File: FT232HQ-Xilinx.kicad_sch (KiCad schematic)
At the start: 33 parts, among them J1 USB_C_Receptacle_USB2.0_16P, J2 Conn_02x07_Odd_Even, J3 Conn_02x05_Odd_Even, U1 TLV9061xDBV, U2 TLV75533PDBV, U3 SN74AVC4T774PW, U4 12M, U5 FT232H, U6 93LCxxBxxOT

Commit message: fix: 1. Add 10k between vref and gnd. 2. Remove vias on pads.
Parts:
- added R1: 10k, Resistor_SMD:R_0402_1005Metric, symbol Device:R
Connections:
- net GND: now also R1.2
- net VREF: now also R1.1
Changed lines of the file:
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@@
 	)
 	(junction
+		(at 207.01 115.57)
+		(diameter 0)
+		(color 0 0 0 0)
+	)
+	(junction
 		(at 193.04 148.59)
 		(diameter 0)
@@
 	)
 	(junction
+		(at 198.12 105.41)
+		(diameter 0)
+		(color 0 0 0 0)
+	)
+	(junction
 		(at 248.92 107.95)
 		(diameter 0)
@@
 	(wire
 		(pts
+			(xy 198.12 107.95) (xy 198.12 105.41)
+		)
+		(stroke
+			(width 0)
+			(type default)
+		)
+	)
+	(wire
+		(pts
 			(xy 52.07 124.46) (xy 63.5 124.46)
 		)
@@
 	(wire
 		(pts
+			(xy 198.12 115.57) (xy 207.01 115.57)
+		)
+		(stroke
+			(width 0)
+			(type default)
+		)
+	)
+	(wire
+		(pts
 			(xy 142.24 132.08) (xy 144.78 132.08)
 		)
@@
 	(wire
 		(pts
+			(xy 198.12 105.41) (xy 201.93 105.41)
+		)
+		(stroke
+			(width 0)
+			(type default)
+		)
+	)
+	(wire
+		(pts
 			(xy 259.08 43.18) (xy 260.35 43.18)
 		)
@@
 	)
 	(symbol
+		(lib_id "Device:R")
+		(at 198.12 111.76 0)
+		(unit 1)
+		(exclude_from_sim no)
+		(in_bom yes)
+		(on_board yes)
+		(dnp no)
+		(property "Reference" "R1"
+			(at 197.358 114.3 90)
+			(effects
+				(font
+					(size 1.27 1.27)
+				)
+				(justify right)
+			)
+		)
+		(property "Value" "10k"
+			(at 198.12 110.236 90)
+			(effects
+				(font
+					(size 1.27 1.27)
+				)
+				(justify right)
+			)
+		)
+		(property "Footprint" "Resistor_SMD:R_0402_1005Metric"
+			(at 196.342 111.76 90)
+			(effects
+				(font
+					(size 1.27 1.27)
+				)
+				(hide yes)
+			)
+		)
+		(property "Datasheet" "~"
+			(at 198.12 111.76 0)
+			(effects
+				(font
+					(size 1.27 1.27)
+				)
+				(hide yes)
+			)
+		)
+		(property "Description" "Resistor"
+			(at 198.12 111.76 0)
+			(effects
+				(font
+					(size 1.27 1.27)
+				)
+				(hide yes)
+			)
+		)
+		(pin "2"
+		)
+		(pin "1"
+		)
+		(instances
+			(project "FT232HQ-Xilinx"
+				(path "/dd4ac3e3-2410-4273-be8c-634c81d8b6b2"
+					(reference "R1")
+					(unit 1)
+				)
+			)
+		)
+	)
+	(symbol
 		(lib_id "power:+3V3")
 		(at 242.57 130.81 90)
@@
 	(symbol
 		(lib_id "power:VCC")
-		(at 201.93 105.41 90)
+		(at 198.12 105.41 90)
 		(unit 1)
 		(exclude_from_sim no)
@@
 		(fields_autoplaced yes)
 		(property "Reference" "#PWR010"
-			(at 205.74 105.41 0)
+			(at 201.93 105.41 0)
 			(effects
 				(font
@@
 		)
 		(property "Value" "VREF"
-			(at 198.12 105.4099 90)
+			(at 194.31 105.4099 90)
 			(effects
 				(font
@@
 		)
 		(property "Footprint" ""
-			(at 201.93 105.41 0)
+			(at 198.12 105.41 0)
 			(effects
 				(font
@@
 		)
 		(property "Datasheet" ""
-			(at 201.93 105.41 0)
+			(at 198.12 105.41 0)
 			(effects
 				(font
@@
 		)
 		(property "Description" "Power symbol creates a global label with name \"VCC\""
-			(at 201.93 105.41 0)
+			(at 198.12 105.41 0)
 			(effects
 				(font

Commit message: update
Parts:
- removed J2: Conn_02x07_Odd_Even, 1st_commonly:Molex_Xilinx_02x07_P2.0mm_Vertical, symbol Connector_Generic:Conn_02x07_Odd_Even
- added C14: 104, Capacitor_SMD:C_0402_1005Metric, symbol Device:C
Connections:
- net +5V: now also C14.1
- net GND: now also C14.2
- no-connect marks 20 -> 17
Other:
- moved on the sheet: R1

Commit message: set ac9 as SLEEP# LED
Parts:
- added D1: LED, LED_SMD:LED_0402_1005Metric, symbol Device:LED
- added R2: 10k, Resistor_SMD:R_0402_1005Metric, symbol Device:R
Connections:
- net +3V3: now also R2.2
- net at U5.33 (ACBUS9): now also D1.1 (K)
- new net: D1.2 (A), R2.1
- no-connect marks 17 -> 16
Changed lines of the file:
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@@
 	)
 	(no_connect
-		(at 160.02 109.22)
-	)
-	(no_connect
 		(at 160.02 86.36)
 	)
@@
 	)
 	(symbol
+		(lib_id "Device:R")
+		(at 171.45 109.22 90)
+		(unit 1)
+		(exclude_from_sim no)
+		(in_bom yes)
+		(on_board yes)
+		(dnp no)
+		(property "Reference" "R2"
+			(at 170.434 107.188 90)
+			(effects
+				(font
+					(size 1.27 1.27)
+				)
+				(justify right)
+			)
+		)
+		(property "Value" "10k"
+			(at 169.926 109.22 90)
+			(effects
+				(font
+					(size 1.27 1.27)
+				)
+				(justify right)
+			)
+		)
+		(property "Footprint" "Resistor_SMD:R_0402_1005Metric"
+			(at 171.45 110.998 90)
+			(effects
+				(font
+					(size 1.27 1.27)
+				)
+				(hide yes)
+			)
+		)
+		(property "Datasheet" "~"
+			(at 171.45 109.22 0)
+			(effects
+				(font
+					(size 1.27 1.27)
+				)
+				(hide yes)
+			)
+		)
+		(property "Description" "Resistor"
+			(at 171.45 109.22 0)
+			(effects
+				(font
+					(size 1.27 1.27)
+				)
+				(hide yes)
+			)
+		)
+		(pin "2"
+		)
+		(pin "1"
+		)
+		(instances
+			(project "FT232HQ-Xilinx"
+				(path "/dd4ac3e3-2410-4273-be8c-634c81d8b6b2"
+					(reference "R2")
+					(unit 1)
+				)
+			)
+		)
+	)
+	(symbol
 		(lib_id "power:VCC")
 		(at 270.51 133.35 270)
@@
 	)
 	(symbol
+		(lib_id "Device:LED")
+		(at 163.83 109.22 0)
+		(unit 1)
+		(exclude_from_sim no)
+		(in_bom yes)
+		(on_board yes)
+		(dnp no)
+		(property "Reference" "D1"
+			(at 163.83 106.68 0)
+			(effects
+				(font
+					(size 1.27 1.27)
+				)
+			)
+		)
+		(property "Value" "LED"
+			(at 163.83 112.522 0)
+			(effects
+				(font
+					(size 1.27 1.27)
+				)
+			)
+		)
+		(property "Footprint" "LED_SMD:LED_0402_1005Metric"
+			(at 163.83 109.22 0)
+			(effects
+				(font
+					(size 1.27 1.27)
+				)
+				(hide yes)
+			)
+		)
+		(property "Datasheet" "~"
+			(at 163.83 109.22 0)
+			(effects
+				(font
+					(size 1.27 1.27)
+				)
+				(hide yes)
+			)
+		)
+		(property "Description" "Light emitting diode"
+			(at 163.83 109.22 0)
+			(effects
+				(font
+					(size 1.27 1.27)
+				)
+				(hide yes)
+			)
+		)
+		(pin "2"
+		)
+		(pin "1"
+		)
+		(instances
+			(project "FT232HQ-Xilinx"
+				(path "/dd4ac3e3-2410-4273-be8c-634c81d8b6b2"
+					(reference "D1")
+					(unit 1)
+				)
+			)
+		)
+	)
+	(symbol
 		(lib_id "Interface_USB:FT232H")
 		(at 137.16 93.98 0)
@@
 					(unit 1)
 				)
+			)
+		)
+	)
+	(symbol
+		(lib_id "power:+5V")
+		(at 175.26 109.22 270)
+		(unit 1)
+		(exclude_from_sim no)
+		(in_bom yes)
+		(on_board yes)
+		(dnp no)
+		(fields_autoplaced yes)
+		(property "Reference" "#PWR018"
+			(at 171.45 109.22 0)
+			(effects
+				(font
+					(size 1.27 1.27)
+				)
+				(hide yes)
+			)
+		)
+		(property "Value" "+3V3"
+			(at 179.07 109.2199 90)
+			(effects
+				(font
+					(size 1.27 1.27)
+				)
+				(justify left)
+			)
+		)
+		(property "Footprint" ""
+			(at 175.26 109.22 0)
+			(effects
+				(font
+					(size 1.27 1.27)
+				)
+				(hide yes)
+			)
+		)
+		(property "Datasheet" ""
+			(at 175.26 109.22 0)
+			(effects
+				(font
+					(size 1.27 1.27)
+				)
+				(hide yes)
+			)
+		)
+		(property "Description" "Power symbol creates a global label with name \"+5V\""
+			(at 175.26 109.22 0)
+			(effects
+				(font
+					(size 1.27 1.27)
+				)
+				(hide yes)
+			)
+		)
+		(pin "1"
+		)
+		(instances
+			(project "FT232HQ-Xilinx"
+				(path "/dd4ac3e3-2410-4273-be8c-634c81d8b6b2"
+					(reference "#PWR018")
+					(unit 1)
+				)

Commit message: remove ldo and useless resistance
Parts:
- removed R11, R12, R9: 10k, Resistor_SMD:R_0402_1005Metric, symbol Device:R
- removed U2: TLV75533PDBV, Package_TO_SOT_SMD:SOT-23-5, symbol Regulator_Linear:TLV75533PDBV
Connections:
- net +3V3: no longer U5.40 (VREGIN)
- net +5V: now also U5.40 (VREGIN)

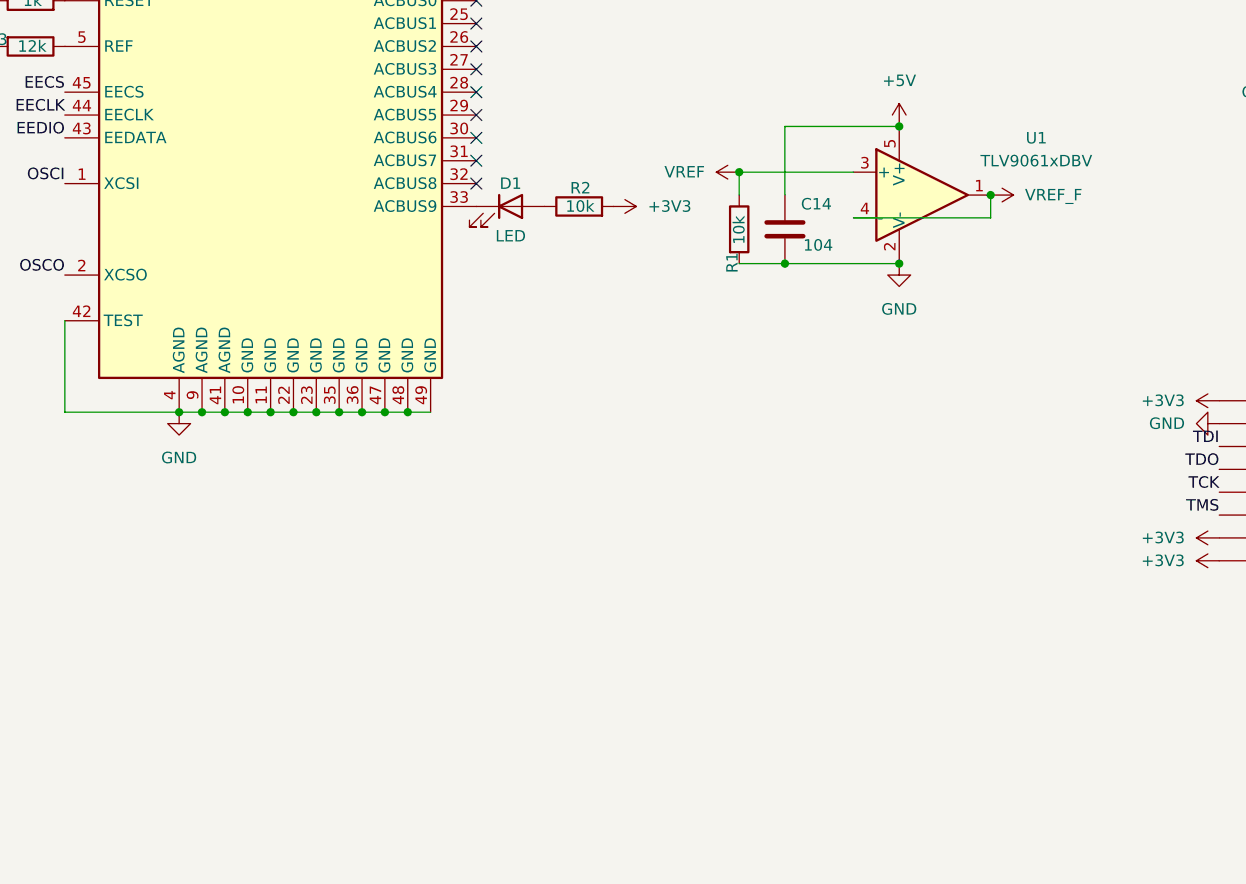
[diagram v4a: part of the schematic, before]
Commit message: add raspberry jst-sh1.0 uart
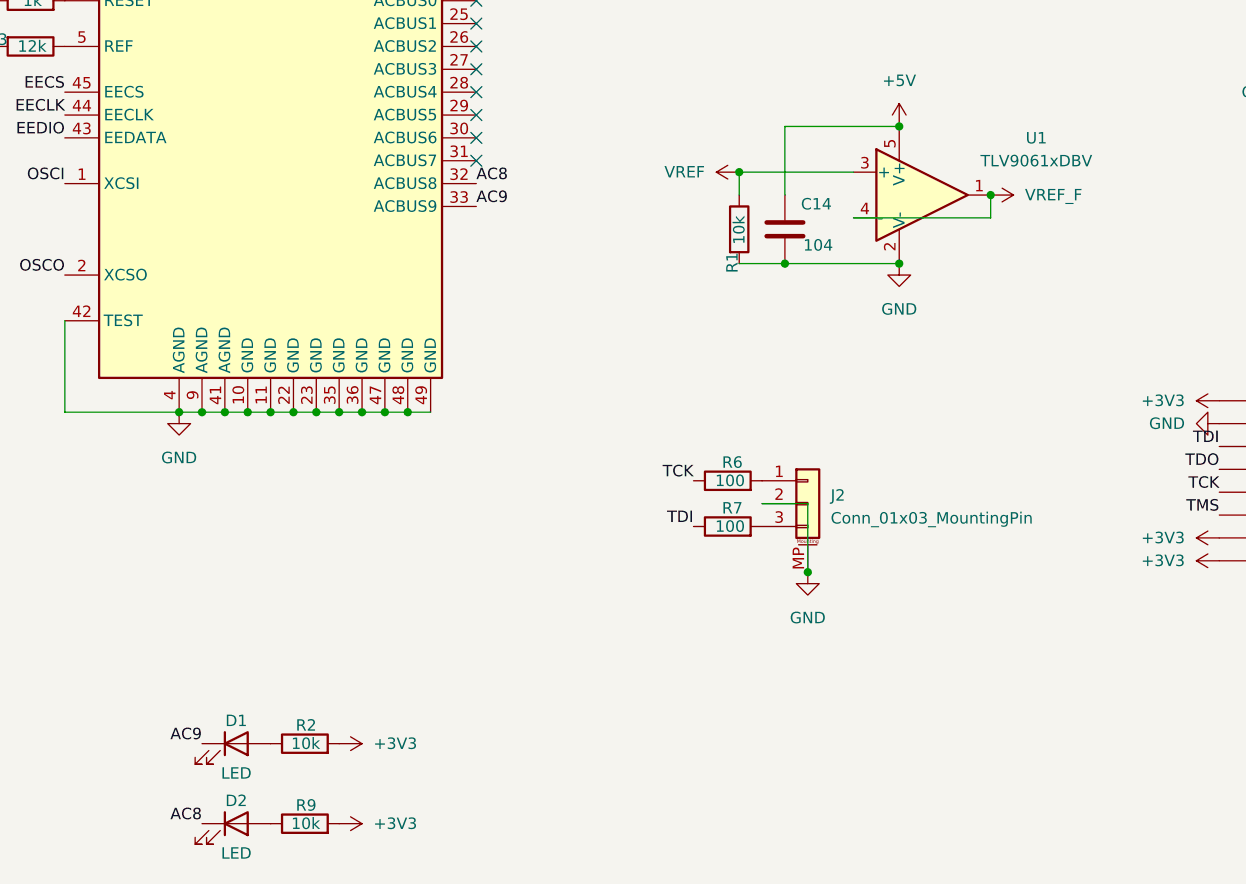
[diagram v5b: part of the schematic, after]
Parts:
- added D2: LED, LED_SMD:LED_0402_1005Metric, symbol Device:LED
- added J2: Conn_01x03_MountingPin, Connector_JST:JST_SH_SM03B-SRSS-TB_1x03-1MP_P1.00mm_Horizontal, symbol Connector_Generic_MountingPin:Conn_01x03_MountingPin
- added R6, R7: 100, Resistor_SMD:R_0402_1005Metric, symbol Device:R
- added R9: 10k, Resistor_SMD:R_0402_1005Metric, symbol Device:R
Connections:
- net +3V3: now also R9.2
- net GND: now also J2.2 (Pin_2), J2.MP (MountPin)
- net TCK: now also R6.1
- net TDI: now also R7.1
- net AC9: now reaches D1.1 (K), U5.33 (ACBUS9)
- net AC8: now reaches U5.32 (ACBUS8)
- net AC8: now also D2.1 (K)
- new net: J2.3 (Pin_3), R7.2
- new net: J2.1 (Pin_1), R6.2
- new net: D2.2 (A), R9.1
- no-connect marks 16 -> 15
